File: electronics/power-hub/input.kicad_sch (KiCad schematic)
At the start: 9 parts, among them J1 24V IN, Q1 SUD50P06-15

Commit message: BOM: bulk hardware prices, JLC PCBA type per board
- hardware at bulk prices (T-nuts, screws, heat-set inserts, corner
  brackets), generic USB-C panel extensions; drop the label tape (the
  printed bay_label fills the drawer recess); heat-set inserts for camera
  pods only where a camera hangs
- catalog: standard_only flag (ESP32-S3-MINI-1, WS2812B-2020 cannot be
  placed with JLC Economic PCBA); bom.py prices Standard PCBA for the
  bay node and Economic for the power hub
- electrolytics moved to the Economic-capable LCSC listings of the same
  parts (C3352, C3358); PCB footprint fields synced, ERC/DRC/parity clean
- docs: JLC assembly notes (no Basic drop-ins for the extended parts)

Total ~EUR 927 -> ~EUR 828 (EUR 66 -> 59 per bay).

Co-Authored-By: Claude Opus 5.5 <noreply@anthropic.com>
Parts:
- C1, C2: LCSC C72499 -> C3358; Manufacturer ROQANG -> Honor Elec
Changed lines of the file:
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@@
 			)
 		)
-		(property "Manufacturer" "ROQANG"
+		(property "Manufacturer" "Honor Elec"
 			(at 193.04 49.53 0)
 			(effects
@@
 			)
 		)
-		(property "LCSC" "C72499"
+		(property "LCSC" "C3358"
 			(at 193.04 49.53 0)
 			(effects
@@
 			)
 		)
-		(property "Manufacturer" "ROQANG"
-			(at 205.74 49.53 0)
-			(effects
-				(font
-					(size 1.27 1.27)
-				)
-				(hide yes)
-			)
-		)
-		(property "LCSC" "C72499"
-			(at 205.74 49.53 0)
-			(effects
+		(property "Manufacturer" "Honor Elec"
+			(at 205.74 49.53 0)
+			(effects
+				(font
+					(size 1.27 1.27)
+				)
+				(hide yes)
+			)
+		)
+		(property "LCSC" "C3358"
+			(at 205.74 49.53 0)
+			(effects

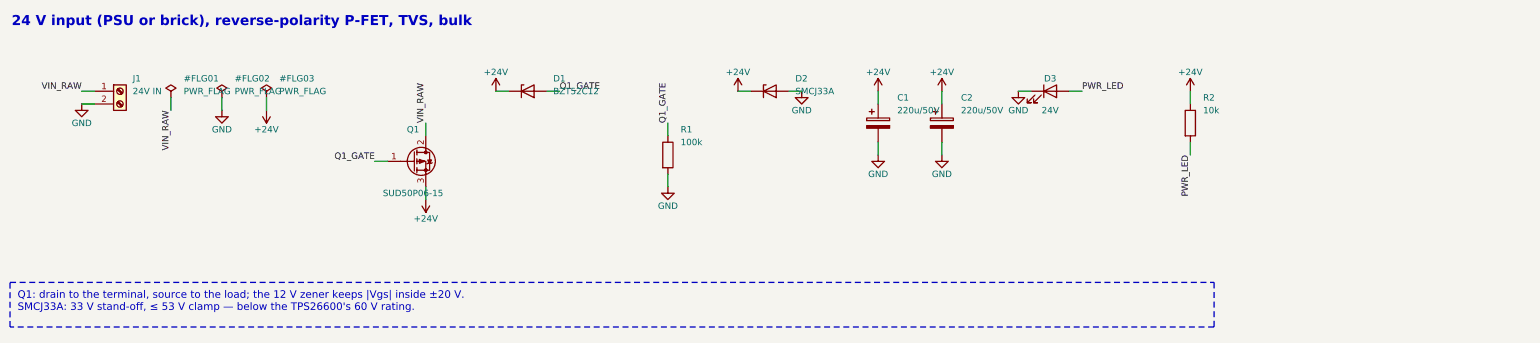
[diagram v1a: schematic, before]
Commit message: Schematics: draw real wires and an overview block diagram
The generator used to connect every pin through a net label only. Now,
in each block, the part with the most pins is the anchor and the
two-pin parts that share a signal with one of its side pins hang off
that pin on a real wire; parts chained behind them (R -> C -> GND)
stack underneath, and anchor-less blocks (pull-ups, reset/boot
buttons) are adopted by the anchor they connect to. Power symbols on
side pins point outward; power-flag references are hidden.

The root sheet becomes a block diagram: the supply rails each sheet
uses across the top, and one lane per pair of sheets listing the
signals they share.

Every wired net still carries one label, so net names, ERC (0) and the
PCB's schematic parity (0) are unchanged; the routed PCBs are untouched.

Co-Authored-By: Claude Opus 5.5 <noreply@anthropic.com>
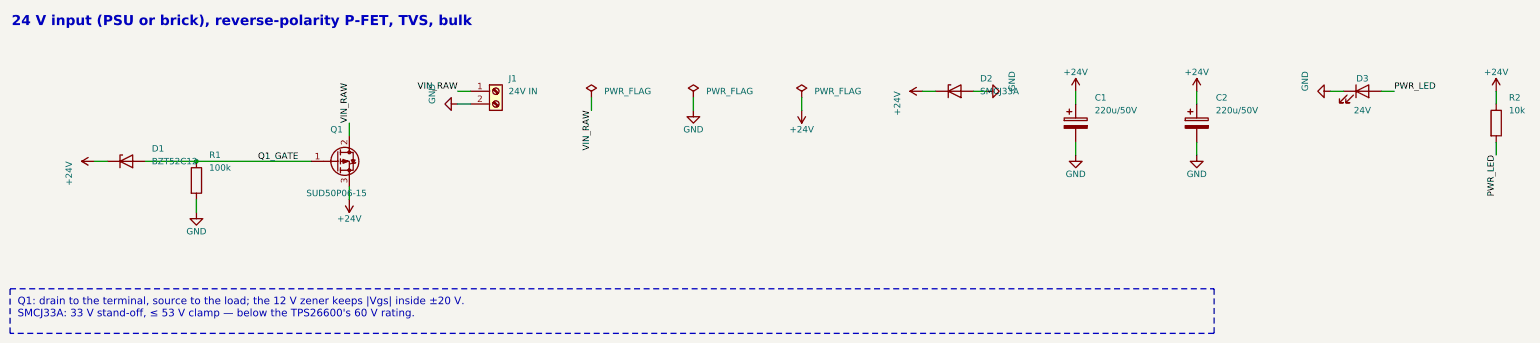
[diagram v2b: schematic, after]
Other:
- moved on the sheet: C1, C2, D1, D2, D3, J1, Q1, R1, R2

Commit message: Boards v0.2: LMR51635 buck, JST PH, drawn schematics, thermal reliefs
Addresses Fabio's review of v0.1.

Bay node (rev 0.2):
- 5 V buck: LMR51635YDDCR (60 V, 3.5 A, synchronous, 1.1 MHz) with a
  3.3 uH FXL0630, 3 x 22 uF out, 2 x 10 uF + 100 nF in, FB 120k/22k
  (5.16 V), EN 1M/100k UVLO (13.5 V on, 10.8 V off). Replaces the
  TPS54360B, its Schottky and compensation network. CIN straddles the
  VIN/GND pins on solid top-side islands with vias to In1 (TI SLUSF64B).
- 24 V in/out on JST PH (carrier notches resized, rack.yaml pwr_y).
- Power nets named along the path: 24V_BUS -> +24V -> +5V -> DUT_5V_SW
  -> shunt -> DUT_5V; the INA226 visibly runs from +3V3.
- Stackup S+GND / GND / PWR / S+GND: In2 carries +5V, +3V3 under the
  ESP32 and a protected 24 V bus strip. Outer GND pours kept (without
  them Freerouting left ~25 connections unrouted).

Power hub (rev 0.2): JST VH input instead of the screw terminal, JST PH
row outputs, eFuse limit 1.6 A (RILIM 7.5k) to protect the 2 A contacts.

Generator:
- eda.py: drawn schematic mode (sch= placement, Sheet.wire/tag/frame,
  rotated/mirrored symbols, automatic junctions, per-island labels and
  checks that no wire touches another net); all seven sheets redrawn.
- pcbgen.py: thermal reliefs on every pour (+ <board>.kicad_dru for
  single spokes on fine pitch), configurable inner layers, per-zone
  deferral, fixed vias, DRC-driven fix-up for isolated GND pads.
- JLC CPL fix for the LMR51635 (270 deg); BOM, cables, viewer, docs.

ERC 0, DRC 0 copper errors, 0 unconnected, schematic parity 0 on both.

Co-Authored-By: Claude Opus 5.5 <noreply@anthropic.com>
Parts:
- J1: footprint TerminalBlock_Phoenix:TerminalBlock_Phoenix_MKDS-1,5-2-5.08_1x02_P5.08mm_Horizontal -> Connector_JST:JST_VH_B2P-VH_1x02_P3.96mm_Vertical; symbol Connector:Screw_Terminal_01x02 -> Connector_Generic:Conn_01x02; LCSC C474952 -> C160315; MPN KF128-5.08-2P-AA -> B2P-VH(LF)(SN); Manufacturer Cixi Kefa -> JST
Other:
- note added: "24 V input (Mean Well PSU or brick, JST VH), reverse-polarity P-FET, TVS, bulk"
- note removed: "24 V input (PSU or brick), reverse-polarity P-FET, TVS, bulk"
- moved on the sheet: C1, C2, D1, D2, D3, Q1, R1, R2

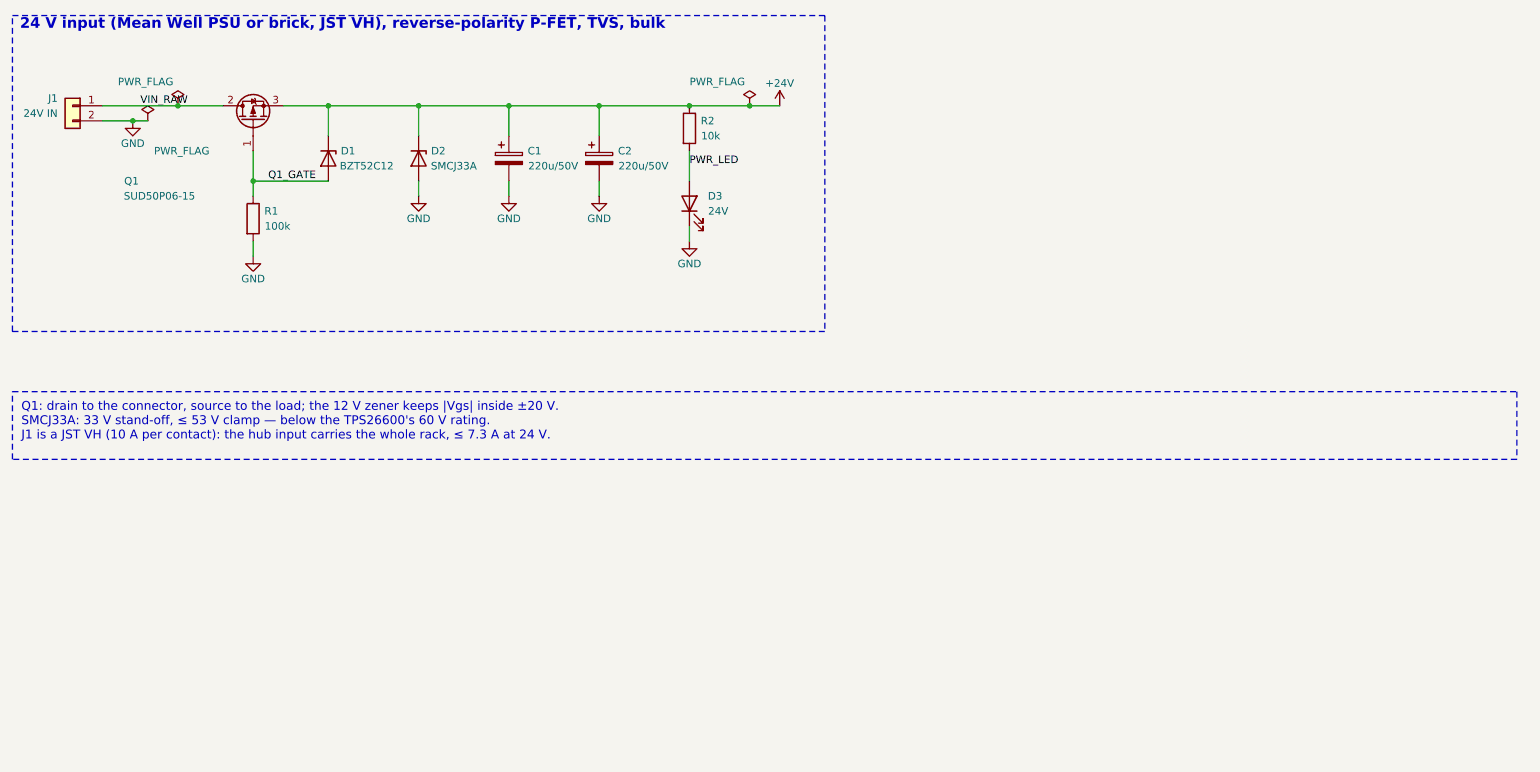
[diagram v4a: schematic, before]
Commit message: Power hub v0.4: eFuses + rack controller (ESP32-S3, CAN master)
A new board for the power box: 76 x 140 mm, 2 layers, drawn around the
outline, holes, row connectors and front LEDs in config/rack.yaml.

- 24 V in on a JST VH (the brick's crimped DC cord), P-FET + TVS + bulk,
  then 4 x TPS26600 (1.6 A) to 6-pin JST PH row outputs: 24 V, GND,
  CAN_H, CAN_L, GND, POS (docs/can.md)
- every row on without firmware (SHDN held high by a 1M/150k divider from
  24 V); the controller can switch a row off (2N7002) and reads FLT and IMON
- rack controller: ESP32-S3-MINI-1, LMR51635 5 V buck (the bay node's
  layout) diode-ORed with USB-C VBUS, AMS1117; TCAN1044AV with both
  terminations of the star bus (2 x 56 ohm split, twice), PESD2CAN; POS per
  row through 10k + BAT54S clamp (survives a reversed cable)
- side-view ON / FAULT LEDs per row, 24V and CTL in the box's front wall
- autorouted; ERC 0, DRC 0, 0 unconnected, parity 0; Konnect review in
  docs/review-konnect.md (VBUS cap added; the rest per-sheet false positives)
- box re-generated for the final hole / connector / LED positions; viewer
  shows the real board; BOM carries an estimate (Standard PCBA, not quoted)
- schematic: automatic block layout for now

Co-Authored-By: Claude Opus 5.5 <noreply@anthropic.com>
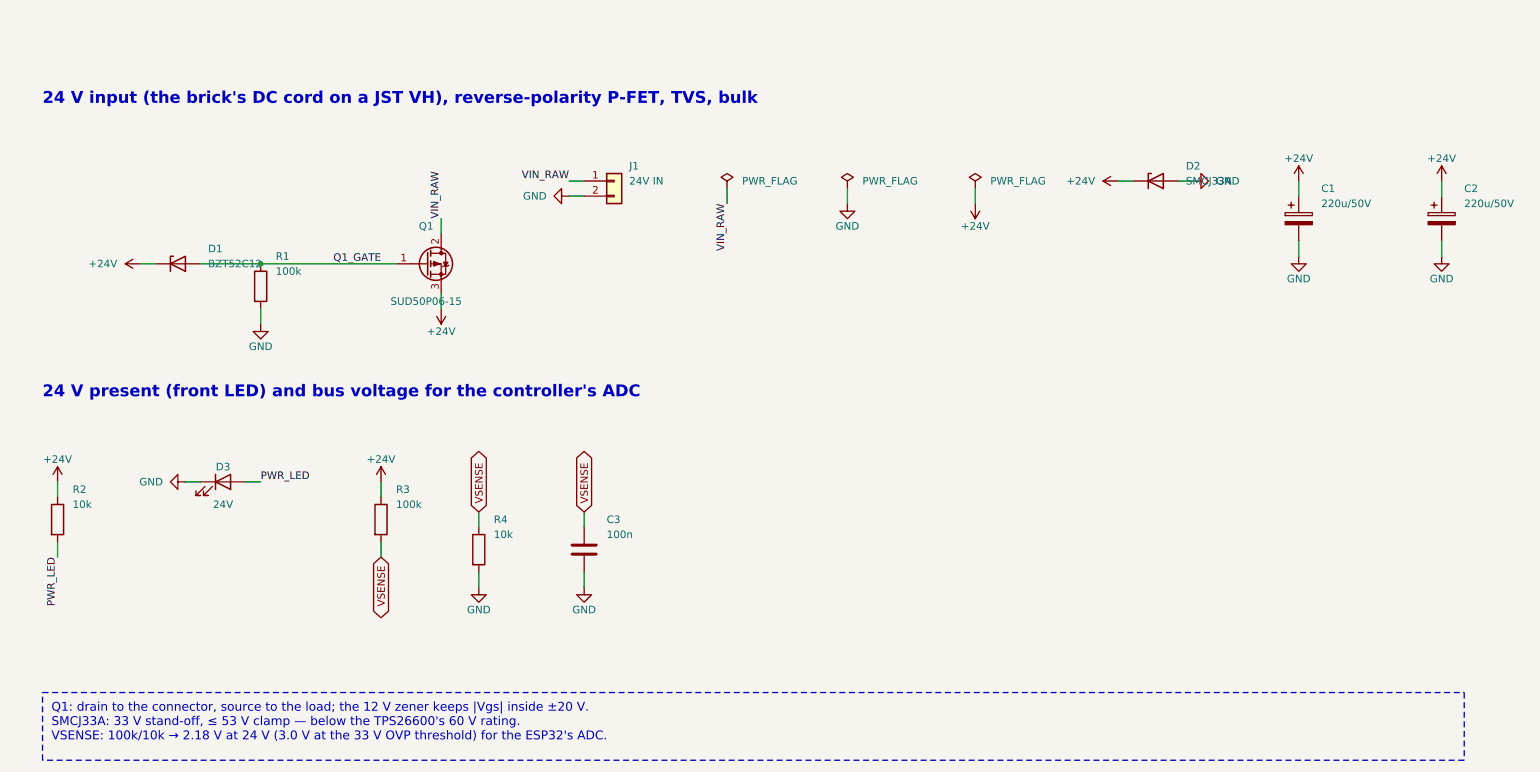
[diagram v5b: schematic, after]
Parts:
- added C3: 100n, Capacitor_SMD:C_0603_1608Metric, symbol Device:C
- added R3: 100k, Resistor_SMD:R_0603_1608Metric, symbol Device:R
- added R4: 10k, Resistor_SMD:R_0603_1608Metric, symbol Device:R
- D3: footprint LED_SMD:LED_0805_2012Metric -> LED_SMD:LED_Kingbright_KPA-3010_3x2x1mm; LCSC C2297 -> C598310; MPN KT-0805G -> KPA-3010CGCK; Manufacturer Hubei KENTO -> Kingbright
- J1: footprint Connector_JST:JST_VH_B2P-VH_1x02_P3.96mm_Vertical -> Connector_JST:JST_VH_S2P-VH_1x02_P3.96mm_Horizontal; LCSC C160315 -> C160355; MPN B2P-VH(LF)(SN) -> S2P-VH(LF)(SN)
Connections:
- net +24V: now also R3.1
- net GND: now also C3.2, R4.2
- new net VSENSE: C3.1, R3.2, R4.1
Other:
- note added: "24 V input (the brick's DC cord on a JST VH), reverse-polarity P-FET, TVS, bulk"
- note added: "24 V present (front LED) and bus voltage for the controller's ADC"
- note removed: "24 V input (Mean Well PSU or brick, JST VH), reverse-polarity P-FET, TVS, bulk"
- moved on the sheet: C1, C2, D1, D2, D3, J1, Q1, R1, R2
